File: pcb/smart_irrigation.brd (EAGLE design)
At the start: 76.2 x 76.2 mm, 31 parts, among them IC1 TMP36, IC2 7805DT, IC3 7833DT, IC4 DS1307, Q1 IRF730, Q2 32.768, Q3 2N3904, U1 BL600

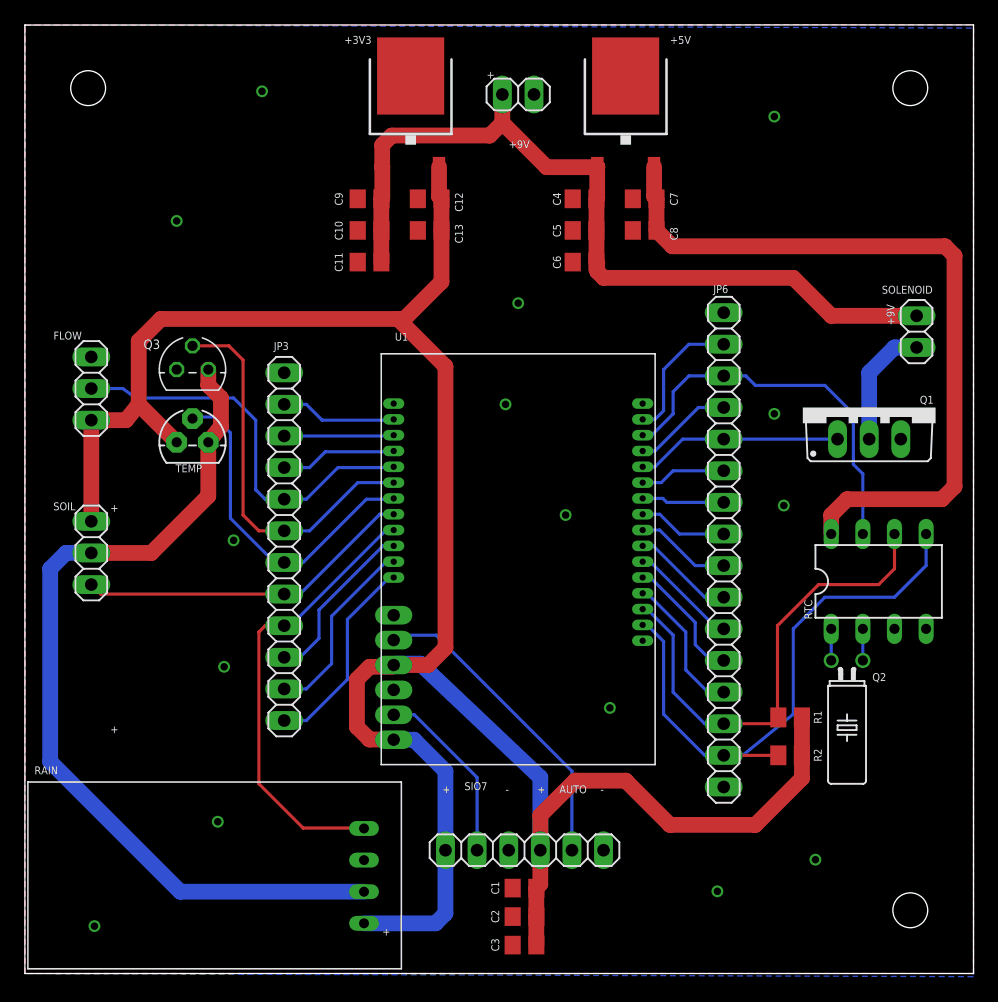
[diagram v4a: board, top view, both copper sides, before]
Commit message: PCB: Add reset button
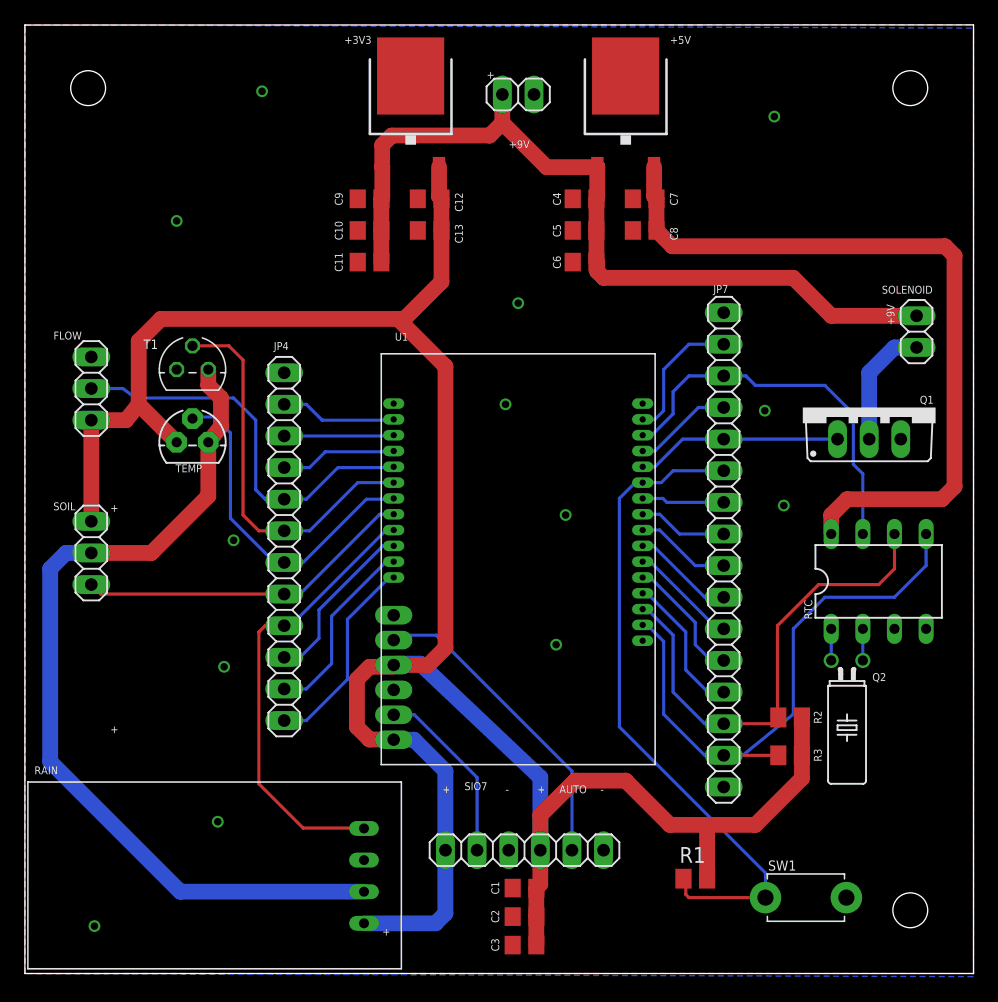
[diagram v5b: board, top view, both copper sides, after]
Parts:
- removed J1: (no value), pinhead:1X02
- added JP8: (no value), pinhead:1X02
- added R3: 2.2k, rcl:M0805
- added SW1: (no value), adafruit:TACT_PANA-EVQ
- JP2: device pinhead:1X03 -> smart_irrigation:1X03
- JP3: device pinhead:1X12 -> pinhead:1X03
- JP4: device pinhead:1X06 -> pinhead:1X12
- JP5: device pinhead:1X02 -> pinhead:1X06
- JP6: device pinhead:1X16 -> pinhead:1X02
- JP7: device smart_irrigation:1X03 -> pinhead:1X16
- R1: value 2.2k -> 10k
- moved JP7 52.4 mm to (56.1, 34.0), turned to 270 degrees
- moved JP5 52.2 mm to (40.1, 9.91), turned to 180 degrees
- moved JP6 40.1 mm to (39.6, 70.6), turned to 180 degrees
- moved JP4 31.1 mm to (20.8, 34.3), turned to 270 degrees
- moved JP3 15.5 mm to (5.33, 33.8)
- moved R1 15.0 mm to (53.8, 7.62)
- moved JP2 13.2 mm to (5.33, 47.0), turned to 90 degrees
- moved R2 3.05 mm to (61.5, 20.6)
- renumbered Q3 to T1
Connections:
- net +3V3: now also JP3.1, JP5.3, JP5.6, R3.2; no longer JP4.3, JP4.6, JP7.1
- net +9V: now also JP6.2, JP8.1; no longer J1.2, JP5.1
- net 3V3_TRAN_COL: now also JP3.2; no longer JP2.2
- net FLOW_DATA: now also JP2.2, JP4.5; no longer JP3.5, JP7.2
- net GND: now also JP2.3, JP5.1, JP5.4, JP7.1, JP7.16, SW1.P$2; no longer J1.1, JP3.1, JP4.4, JP6.16, JP7.3
- net NAUTORUN: now also JP5.2; no longer JP4.2
- net NRESET: now also JP7.6, R1.1, SW1.P$1; no longer JP6.6
- net RAIN_DATA: now also JP4.9; no longer JP3.9
- net RTC_DATA: now also JP7.3; no longer JP6.3
- net SCL: now also JP7.14, R2.1; no longer JP6.14, R1.1
- net SDA: now also JP7.15, R3.1; no longer JP6.15, R2.1
- net SENSORS_ENABLE: now also JP4.6; no longer JP3.6
- net SIO_10/MOSI: now also JP7.13; no longer JP6.13
- net SIO_11/MISO: now also JP7.12; no longer JP6.12
- net SIO_12/SCK: now also JP7.11; no longer JP6.11
- net SIO_13: now also JP7.10; no longer JP6.10
- net SIO_14: now also JP7.9; no longer JP6.9
- net SIO_15: now also JP7.8; no longer JP6.8
- net SIO_16: now also JP7.7; no longer JP6.7
- net SIO_18: now also JP7.4; no longer JP6.4
- net SIO_20: now also JP7.2; no longer JP6.2
- net SIO_25: now also JP4.2; no longer JP3.2
- net SIO_26: now also JP4.3; no longer JP3.3
- net SIO_27: now also JP4.4; no longer JP3.4
- net SIO_4: now also JP4.10; no longer JP3.10
- net SIO_5: now also JP4.11; no longer JP3.11
- net SIO_6: now also JP4.12; no longer JP3.12
- net SIO_7: now also JP5.5; no longer JP4.5
- net SOIL_DATA: now also JP3.3, JP4.8; no longer JP2.3, JP3.8
- net SOL_DRAIN: now also JP8.2; no longer JP5.2
- net SOL_ENABLE: now also JP7.5; no longer JP6.5
- net TEMP_DATA: now also JP4.7; no longer JP3.7
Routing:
- net NRESET: track 6.91 -> 54.1 mm
- net +3V3: track 186.4 -> 190.7 mm

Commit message: PCB: Change sensor pin assignments
All digital sensor outputs are now in one cluster and all analog sensor
outputs are in another cluster.
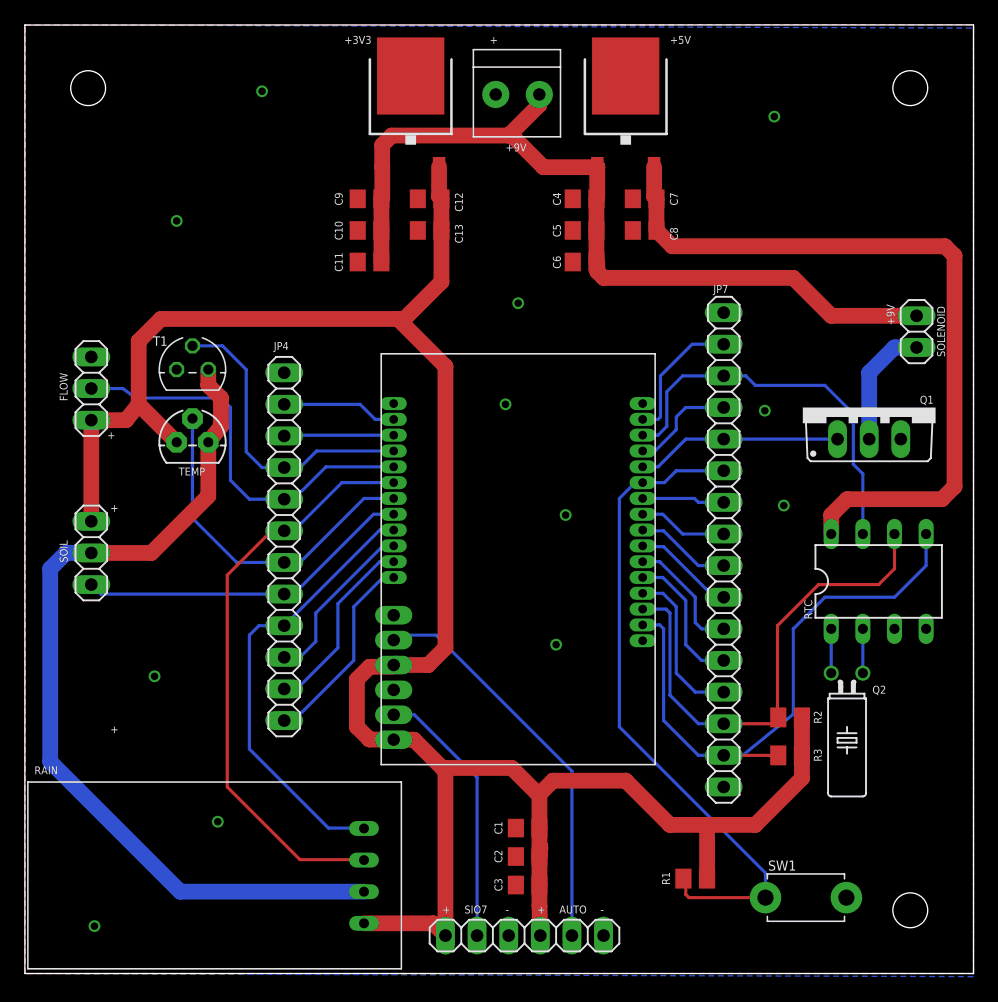
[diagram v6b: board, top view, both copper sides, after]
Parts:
- JP6: value (none) -> 1X2-3.5MM; device pinhead:1X02 -> adafruit:1X2-3.5MM
- moved JP5 6.86 mm to (40.1, 3.05)
- moved C3 4.83 mm to (40.4, 7.11)
- moved C1 4.83 mm to (40.4, 11.7)
- moved C2 4.83 mm to (40.4, 9.40)
- moved Q2 1.02 mm to (66.0, 24.1)
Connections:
- net RAIN_DATA renamed RAIN_DATA_A
- removed net SIO_27: JP4.4, U1.39
- new net RAIN_DATA_D: JP1.3, JP4.6, U1.42
- net SENSORS_ENABLE: now also JP4.4, U1.39; no longer JP4.6, U1.42
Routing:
- net RAIN_DATA_D: track 0.00 -> 46.9 mm
- net +3V3: track 190.7 -> 181.3 mm
- net SIO_27: track 9.35 -> 0.00 mm
- net SIO_7: track 14.6 -> 21.5 mm
- net NAUTORUN: track 25.4 -> 32.3 mm
- net SENSORS_ENABLE: track 31.2 -> 24.6 mm
- net SIO_10/MOSI: track 11.6 -> 12.9 mm
- net SIO_12/SCK: track 8.75 -> 9.94 mm
- net SCL: track 39.1 -> 40.3 mm
- net +9V: track 66.9 -> 68.0 mm
- net SIO_11/MISO: track 10.3 -> 11.4 mm
- net N$3: track 2.54 -> 3.56 mm
- net N$1: track 2.54 -> 3.56 mm
- net SDA: track 47.6 -> 48.5 mm
- net SIO_18: track 7.96 -> 8.55 mm
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
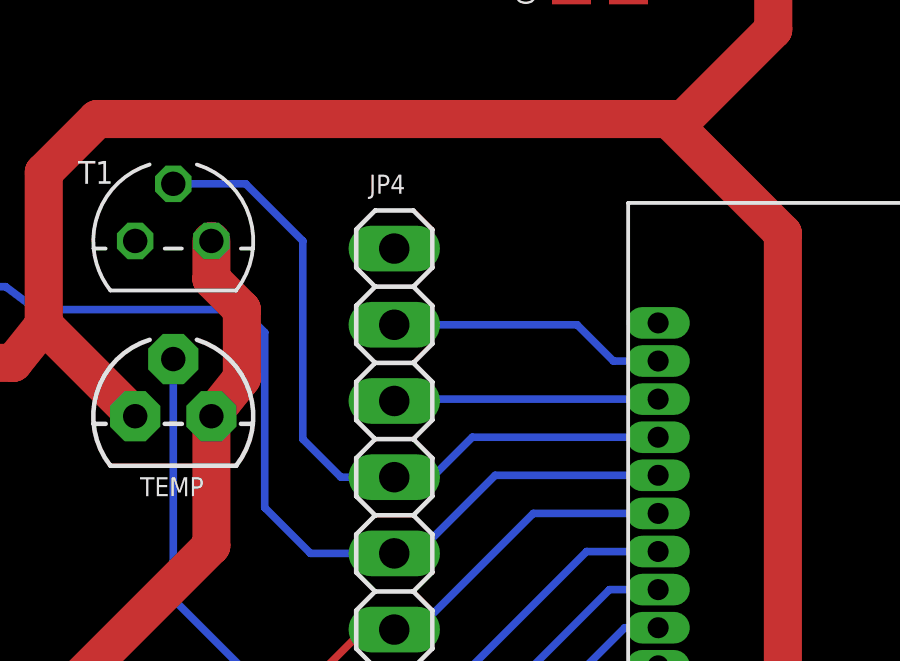
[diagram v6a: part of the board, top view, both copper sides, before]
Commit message: PCB: Change SENSORS_ENABLE signal pin
The BL600 breakout board includes SIO_26 and SIO_27, but they're
reserved and unusable for some reason. SENSORS_ENABLE was thus changed
from SIO_27 to SIO_25.
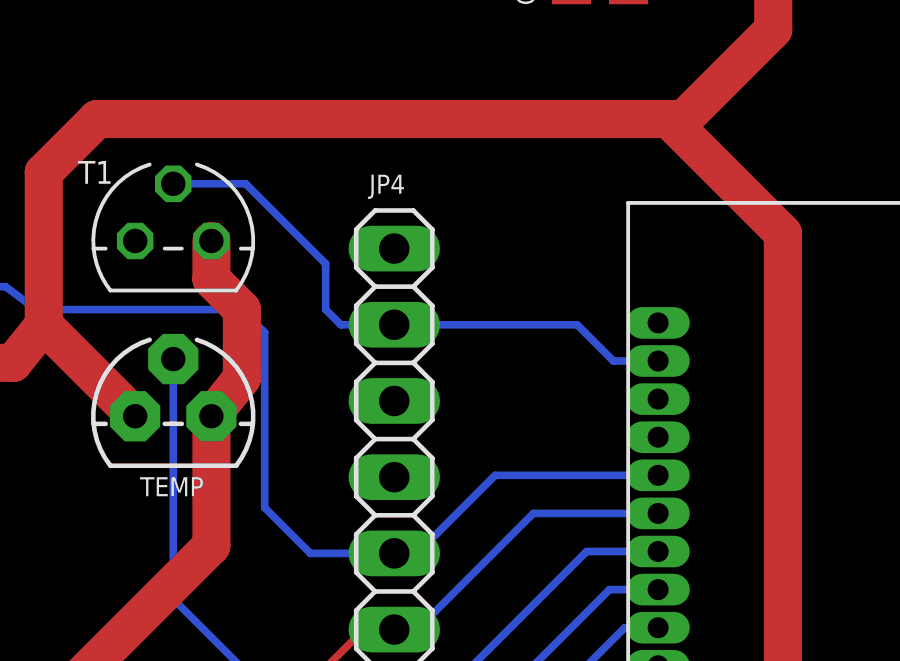
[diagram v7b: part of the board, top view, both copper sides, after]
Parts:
- C1, C2: value 10uF -> 0.1uF
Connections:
- removed net SIO_25: JP4.2, U1.36
- removed net SIO_26: JP4.3, U1.38
- net SENSORS_ENABLE: now also JP4.2, U1.36; no longer JP4.4, U1.39
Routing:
- net SIO_25: track 9.30 -> 0.00 mm
- net SIO_26: track 8.82 -> 0.00 mm
- net SENSORS_ENABLE: track 24.6 -> 19.5 mm
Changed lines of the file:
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@@
 <?xml version="1.0" encoding="utf-8"?>
 <!DOCTYPE eagle SYSTEM "eagle.dtd">
-<eagle version="7.3.0">
+<eagle version="7.5.0">
 <drawing>
 <settings>
@@
 <attribute name="VALUE" x="30.24" y="17.382" size="1.27" layer="27" rot="R180"/>
 </element>
-<element name="C1" library="rcl" package="C0805" value="10uF" x="40.386" y="11.684" smashed="yes" rot="R180">
+<element name="C1" library="rcl" package="C0805" value="0.1uF" x="40.386" y="11.684" smashed="yes" rot="R180">
 <attribute name="NAME" x="38.354" y="11.176" size="0.635" layer="25" font="vector" ratio="20" rot="R90"/>
 </element>
-<element name="C2" library="rcl" package="C0805" value="10uF" x="40.386" y="9.398" smashed="yes" rot="R180">
+<element name="C2" library="rcl" package="C0805" value="0.1uF" x="40.386" y="9.398" smashed="yes" rot="R180">
 <attribute name="NAME" x="38.354" y="8.89" size="0.635" layer="25" font="vector" ratio="20" rot="R90"/>
 </element>
@@
 <wire x1="31.288" y1="20.782" x2="29.624" y2="20.782" width="0.254" layer="16"/>
 </signal>
-<signal name="SIO_25">
-<contactref element="JP4" pad="2"/>
-<contactref element="U1" pad="36"/>
-<wire x1="29.624" y1="44.512" x2="28.132" y2="44.512" width="0.254" layer="16"/>
-<wire x1="28.132" y1="44.512" x2="26.924" y2="45.72" width="0.254" layer="16"/>
-<wire x1="26.924" y1="45.72" x2="20.828" y2="45.72" width="0.254" layer="16"/>
-</signal>
-<signal name="SIO_26">
-<contactref element="U1" pad="38"/>
-<contactref element="JP4" pad="3"/>
-<wire x1="29.624" y1="43.242" x2="20.89" y2="43.242" width="0.254" layer="16"/>
-<wire x1="20.89" y1="43.242" x2="20.828" y2="43.18" width="0.254" layer="16"/>
-</signal>
 <signal name="FLOW_DATA">
 <contactref element="JP2" pad="2"/>
@@
 <contactref element="JP4" pad="5"/>
 <contactref element="U1" pad="41"/>
-<wire x1="15.748" y1="46.228" x2="16.002" y2="46.228" width="0.254" layer="16"/>
 <wire x1="29.624" y1="40.702" x2="24.192" y2="40.702" width="0.254" layer="16"/>
 <wire x1="24.192" y1="40.702" x2="21.59" y2="38.1" width="0.254" layer="16"/>
@@
 </signal>
 <signal name="SENSORS_ENABLE">
-<contactref element="U1" pad="39"/>
-<contactref element="JP4" pad="4"/>
 <contactref element="T1" pad="2"/>
-<wire x1="29.624" y1="41.972" x2="23.43" y2="41.972" width="0.254" layer="16"/>
-<wire x1="23.43" y1="41.972" x2="22.098" y2="40.64" width="0.254" layer="16"/>
-<wire x1="22.098" y1="40.64" x2="20.828" y2="40.64" width="0.254" layer="16"/>
 <wire x1="13.462" y1="50.419" x2="15.875" y2="50.419" width="0.254" layer="16"/>
-<wire x1="15.875" y1="50.419" x2="17.78" y2="48.514" width="0.254" layer="16"/>
-<wire x1="17.78" y1="48.514" x2="17.78" y2="41.91" width="0.254" layer="16"/>
-<wire x1="17.78" y1="41.91" x2="19.05" y2="40.64" width="0.254" layer="16"/>
-<wire x1="19.05" y1="40.64" x2="20.828" y2="40.64" width="0.254" layer="16"/>
+<contactref element="JP4" pad="2"/>
+<contactref element="U1" pad="36"/>
+<wire x1="29.624" y1="44.512" x2="28.132" y2="44.512" width="0.254" layer="16"/>
+<wire x1="28.132" y1="44.512" x2="26.924" y2="45.72" width="0.254" layer="16"/>
+<wire x1="26.924" y1="45.72" x2="20.828" y2="45.72" width="0.254" layer="16"/>
+<wire x1="15.875" y1="50.419" x2="18.542" y2="47.752" width="0.254" layer="16"/>
+<wire x1="18.542" y1="47.752" x2="18.542" y2="46.228" width="0.254" layer="16"/>
+<wire x1="18.542" y1="46.228" x2="19.05" y2="45.72" width="0.254" layer="16"/>
+<wire x1="19.05" y1="45.72" x2="20.828" y2="45.72" width="0.254" layer="16"/>
 </signal>
 <signal name="SOIL_DATA">

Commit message: PCB: Ground VBAT pin of RTC
Per datasheet, if VBAT is unused, it must be grounded.
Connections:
- removed net VBAT: IC4.3
- net GND: now also IC4.3
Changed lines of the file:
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@@
 <contactref element="SW1" pad="P$2"/>
 <via x="59.436" y="45.212" extent="1-16" drill="0.6"/>
+<contactref element="IC4" pad="3"/>
 </signal>
 <signal name="+9V">
@@
 <wire x1="54.102" y1="17.526" x2="56.134" y2="17.526" width="0.254" layer="16"/>
 </signal>
-<signal name="VBAT">
-<contactref element="IC4" pad="3"/>
-</signal>
 <signal name="SOL_DRAIN">
